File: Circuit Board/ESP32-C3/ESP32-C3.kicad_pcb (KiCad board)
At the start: 2 copper layers, 44 x 58.6 mm, 57 parts, among them IC1 W25Q16JVUXIQ_TR, J1 Conn_01x04_Male, J2 USB_C_Receptacle_USB2.0, SW1 SW_Push, SW2 SW_Push, U1 USBLC6-2SC6, U2 ESP32-C3, U3 USBLC6-2SC6, U4 SPX3819M5-L-3-3

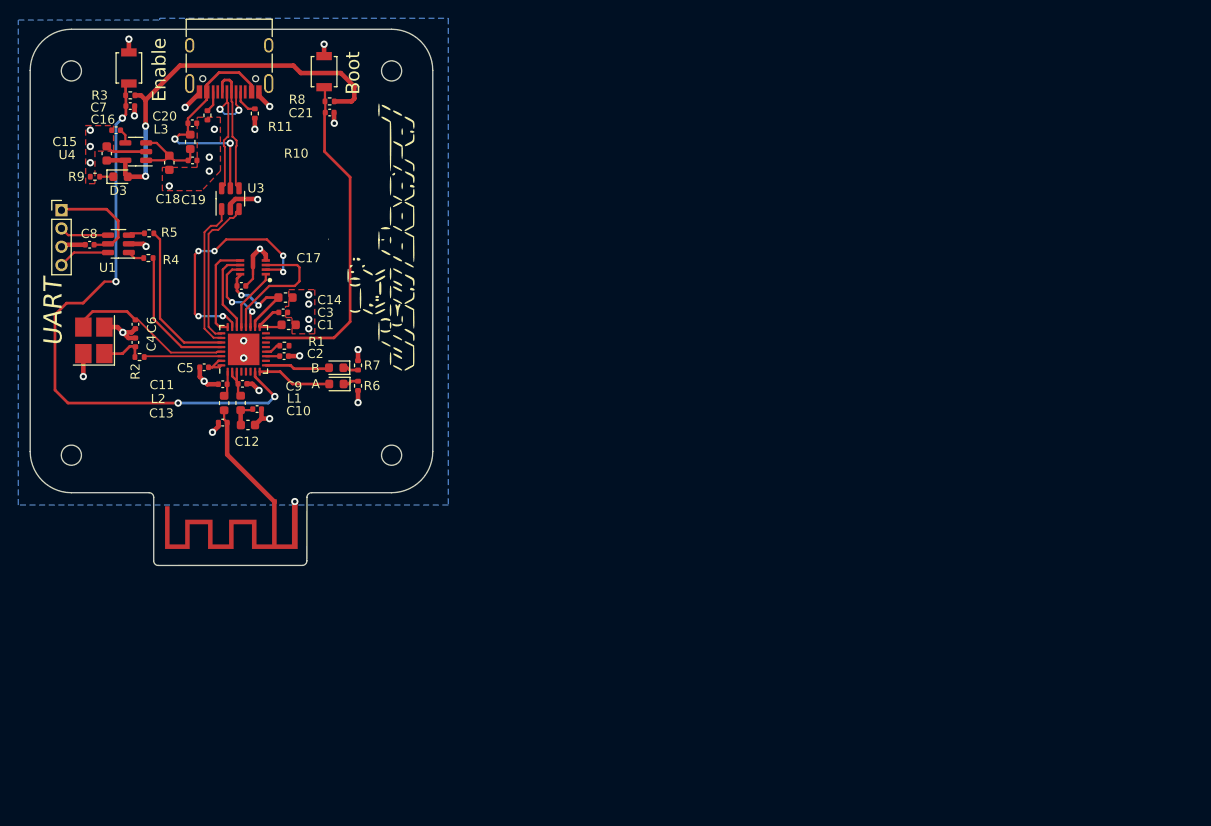
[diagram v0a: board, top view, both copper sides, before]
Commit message: Quick PCB Alignment
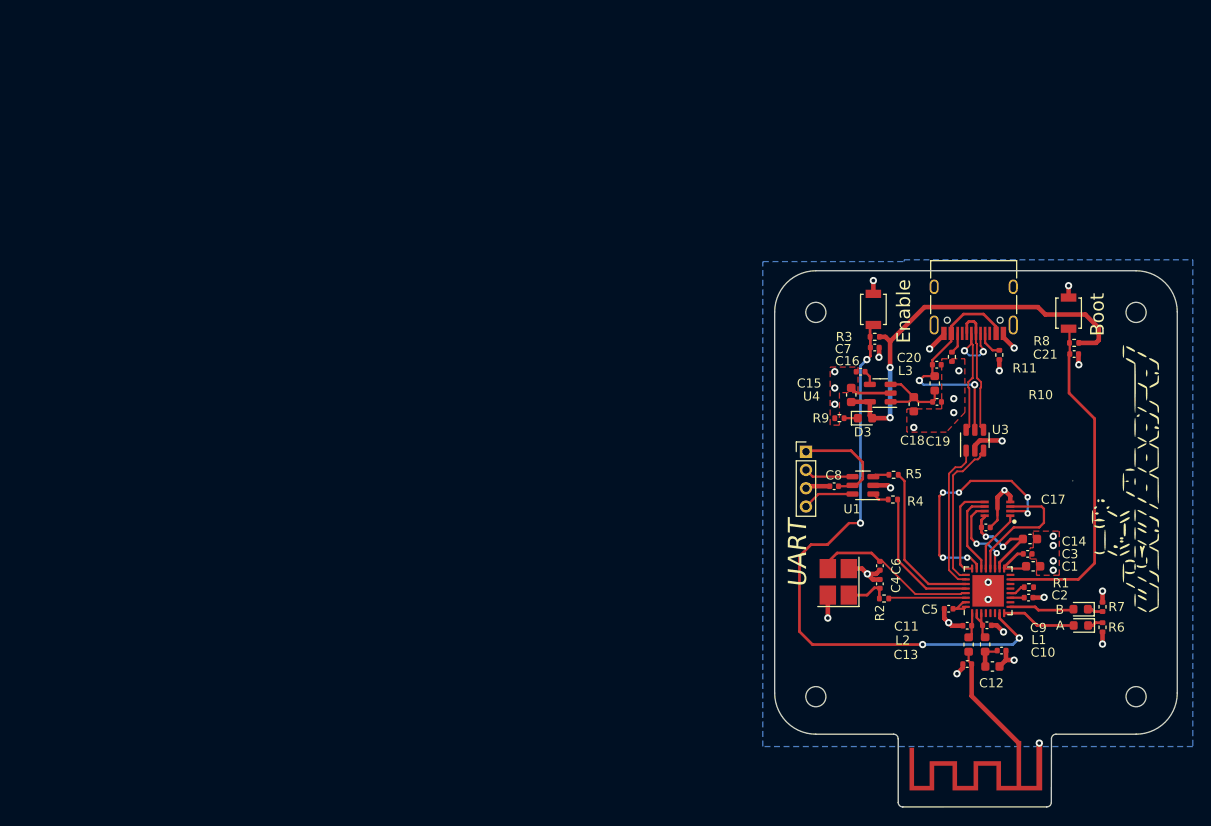
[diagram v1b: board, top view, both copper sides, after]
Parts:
- moved G*** 86.8 mm to (168.2, 83.6), turned to -90 degrees
- moved B 85.5 mm to (160.3, 98.8)
- moved C18 85.5 mm to (142.1, 76.4)
- moved D3 85.5 mm to (136.7, 78.0)
- moved R3 85.5 mm to (137.8, 69.1)
- moved R4 85.5 mm to (139.8, 86.8)
- moved R6 85.5 mm to (162.7, 100.8)
- moved R7 85.5 mm to (162.7, 98.6)
- moved ANT1 85.5 mm to (153.4, 113.5)
- moved C1 85.5 mm to (155.1, 94.1)
- moved C11 85.5 mm to (147.9, 100.6)
- moved C13 85.5 mm to (147.9, 104.8)
- moved C14 85.5 mm to (154.8, 91.2)
- moved C15 85.5 mm to (135.2, 75.4)
- moved C16 85.5 mm to (136.3, 72.9)
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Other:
- outline, holes or cut-outs redrawn
